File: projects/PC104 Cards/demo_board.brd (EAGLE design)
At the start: 90.2 x 95.9 mm, 17 parts, among them J2 M22-6013005, U2 ESP32-DEVKITC-32D

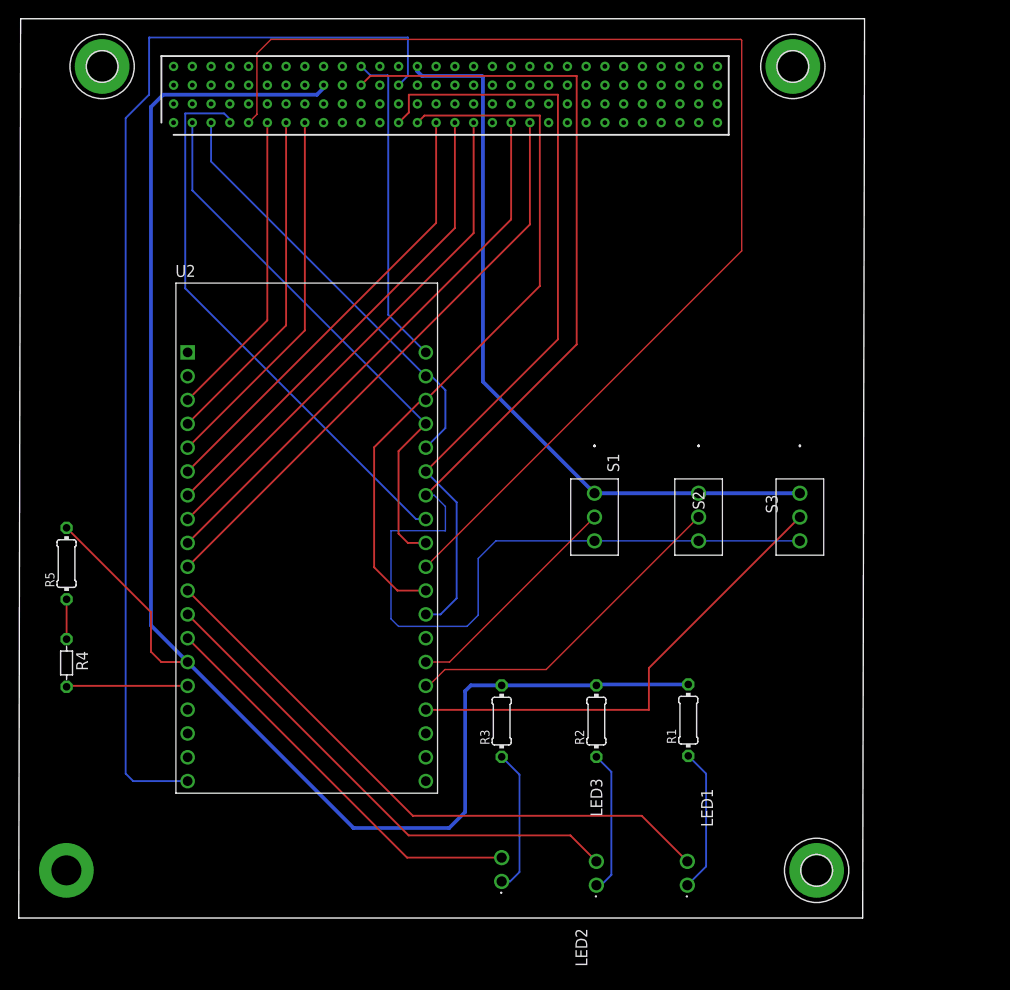
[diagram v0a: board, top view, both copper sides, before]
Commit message: Updated PCB desgins to fix wiring mismatches
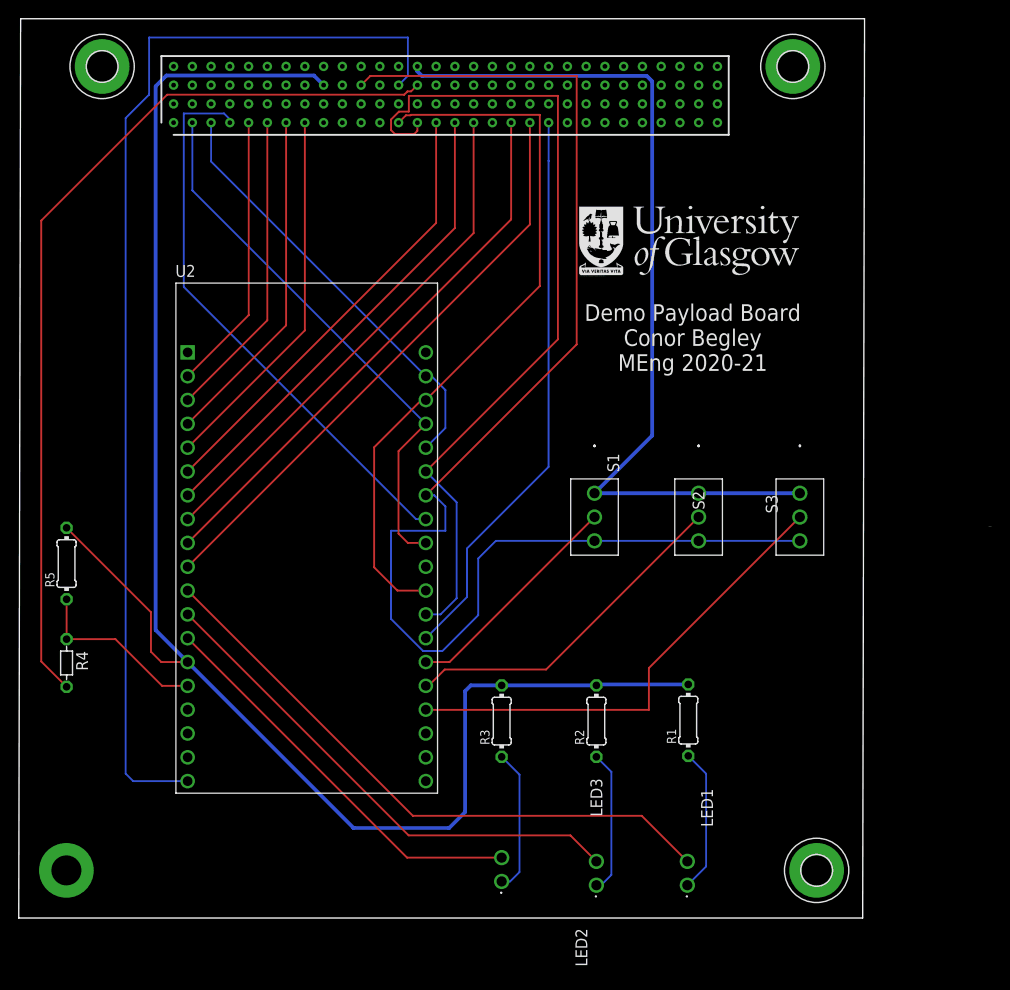
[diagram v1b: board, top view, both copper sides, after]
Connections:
- removed net ADC2: U2.32
- removed net EN: U2.2
- removed net N$2: R4.1, R5.1
- new net DONTCONNECT: U2.20
- net 3V3: now also R4.2
- net ADC: now also U2.32
- net GND5: no longer U2.20
- net GPIO: now also U2.2; no longer U2.29
- net SCL: now also J2.P$103; no longer J2.P$104
- net SDA: now also J2.P$104; no longer J2.P$103
- net THERM: now also R4.1, R5.1; no longer R4.2
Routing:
- net GPIO: track 130.2 -> 29.7 mm
- net 3V3: track 0.00 -> 96.9 mm
- net ADC: track 0.00 -> 60.4 mm
- net GND5: track 34.5 -> 0.00 mm
- net 3V31: track 79.0 -> 94.4 mm
- net THERM: track 13.0 -> 19.2 mm
- net SDA: track 84.2 -> 89.7 mm
- net N$2: track 4.25 -> 0.00 mm
- net GND4: track 146.4 -> 148.6 mm
- net SCL: track 75.7 -> 77.8 mm
- net GND3: track 176.3 -> 177.6 mm
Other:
- board text added: "C:/Users/Conor Begley/Documents/EAGLE/projects/FlatSat/glasgow-caledonian-logoW.bmp"
- board text added: "Demo Payload Board Conor Begley MEng 2020-21"
